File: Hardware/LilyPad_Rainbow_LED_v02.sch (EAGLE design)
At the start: 29 parts

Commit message: Updated Board and Schemtic Files
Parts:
- R1, R2, R3, R4, R5, R6, R7: value 180 -> 150; device SparkFun-Resistors:180OHM1/10W1%(0603) -> SparkFun-Resistors:150OHM-1/10W-1%(0603)
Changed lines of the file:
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@@
 <part name="ST1" library="LilyPad-Wearables" deviceset="SEWTAP" device="6" value="ST +"/>
 <part name="ST" library="LilyPad-Wearables" deviceset="SEWTAP" device="6" value="ST -"/>
-<part name="R1" library="SparkFun-Resistors" deviceset="180OHM1/10W1%(0603)" device="" value="180"/>
+<part name="R1" library="SparkFun-Resistors" deviceset="150OHM-1/10W-1%(0603)" device="" value="150"/>
 <part name="D1" library="SparkFun-LED" deviceset="LED-WHITE" device="1206" value="WHITE"/>
 <part name="ST2" library="LilyPad-Wearables" deviceset="SEWTAP" device="6" value="ST +"/>
 <part name="ST3" library="LilyPad-Wearables" deviceset="SEWTAP" device="6" value="ST -"/>
-<part name="R2" library="SparkFun-Resistors" deviceset="180OHM1/10W1%(0603)" device="" value="180"/>
+<part name="R2" library="SparkFun-Resistors" deviceset="150OHM-1/10W-1%(0603)" device="" value="150"/>
 <part name="D2" library="SparkFun-LED" deviceset="LED-PINK" device="1206" value="PINK"/>
 <part name="ST4" library="LilyPad-Wearables" deviceset="SEWTAP" device="6" value="ST +"/>
 <part name="ST5" library="LilyPad-Wearables" deviceset="SEWTAP" device="6" value="ST -"/>
-<part name="R3" library="SparkFun-Resistors" deviceset="180OHM1/10W1%(0603)" device="" value="180"/>
+<part name="R3" library="SparkFun-Resistors" deviceset="150OHM-1/10W-1%(0603)" device="" value="150"/>
 <part name="D3" library="SparkFun-LED" deviceset="LED-RED" device="LILYPAD" value="RED"/>
 <part name="ST6" library="LilyPad-Wearables" deviceset="SEWTAP" device="6" value="ST +"/>
 <part name="ST7" library="LilyPad-Wearables" deviceset="SEWTAP" device="6" value="ST -"/>
-<part name="R4" library="SparkFun-Resistors" deviceset="180OHM1/10W1%(0603)" device="" value="180"/>
+<part name="R4" library="SparkFun-Resistors" deviceset="150OHM-1/10W-1%(0603)" device="" value="150"/>
 <part name="D4" library="SparkFun-LED" deviceset="LED-YELLOW" device="LILYPAD" value="Yellow"/>
 <part name="ST8" library="LilyPad-Wearables" deviceset="SEWTAP" device="6" value="ST +"/>
 <part name="ST9" library="LilyPad-Wearables" deviceset="SEWTAP" device="6" value="ST -"/>
-<part name="R5" library="SparkFun-Resistors" deviceset="180OHM1/10W1%(0603)" device="" value="180"/>
+<part name="R5" library="SparkFun-Resistors" deviceset="150OHM-1/10W-1%(0603)" device="" value="150"/>
 <part name="D5" library="SparkFun-LED" deviceset="LED-GREEN" device="LILYPAD" value="GREEN"/>
 <part name="ST10" library="LilyPad-Wearables" deviceset="SEWTAP" device="6" value="ST +"/>
 <part name="ST11" library="LilyPad-Wearables" deviceset="SEWTAP" device="6" value="ST -"/>
-<part name="R6" library="SparkFun-Resistors" deviceset="180OHM1/10W1%(0603)" device="" value="180"/>
+<part name="R6" library="SparkFun-Resistors" deviceset="150OHM-1/10W-1%(0603)" device="" value="150"/>
 <part name="D6" library="SparkFun-LED" deviceset="LED-BLUE" device="1206" value="BLUE"/>
 <part name="ST12" library="LilyPad-Wearables" deviceset="SEWTAP" device="6" value="ST +"/>
 <part name="ST13" library="LilyPad-Wearables" deviceset="SEWTAP" device="6" value="ST -"/>
-<part name="R7" library="SparkFun-Resistors" deviceset="180OHM1/10W1%(0603)" device="" value="180"/>
+<part name="R7" library="SparkFun-Resistors" deviceset="150OHM-1/10W-1%(0603)" device="" value="150"/>
 <part name="D7" library="SparkFun-LED" deviceset="LED-WHITE" device="1206" value="WHITE"/>
 <part name="FRAME1" library="SparkFun-Aesthetics" deviceset="FRAME-LETTER" device=""/>

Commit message: updated Board and Schematic files
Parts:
- added U$1: REVISION, SparkFun-Aesthetics:REVISION
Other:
- note added: "Leah Buechley"
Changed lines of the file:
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@@
 <part name="D7" library="SparkFun-LED" deviceset="LED-WHITE" device="1206" value="WHITE"/>
 <part name="FRAME1" library="SparkFun-Aesthetics" deviceset="FRAME-LETTER" device=""/>
+<part name="U$1" library="SparkFun-Aesthetics" deviceset="REVISION" device=""/>
 </parts>
 <sheets>
@@
 <plain>
 <text x="121.92" y="106.68" size="3.81" layer="97" font="vector"></text>
-<text x="167.64" y="10.16" size="2.54" layer="94">Mary West </text>
+<text x="171.45" y="7.62" size="2.54" layer="94">Mary West </text>
 <text x="238.76" y="7.62" size="1.778" layer="94">v02</text>
+<text x="166.37" y="11.43" size="2.54" layer="94">Leah Buechley</text>
 </plain>
 <instances>
@@
 <instance part="FRAME1" gate="G$1" x="0" y="0"/>
 <instance part="FRAME1" gate="V" x="147.32" y="0"/>
+<instance part="U$1" gate="G$1" x="149.86" y="7.62"/>
 </instances>
 <busses>

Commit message: updated fies
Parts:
- added LOGO1: OSHW-LOGOM-COPPER, SparkFun-Aesthetics:OSHW-LOGOM-COPPER
- added LOGO2: SFE_LOGO_NAME_FLAME.1_INCH, SparkFun-Aesthetics:SFE_LOGO_NAME_FLAME.1_INCH
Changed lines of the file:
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@@
 <part name="FRAME1" library="SparkFun-Aesthetics" deviceset="FRAME-LETTER" device=""/>
 <part name="U$1" library="SparkFun-Aesthetics" deviceset="REVISION" device=""/>
+<part name="LOGO2" library="SparkFun-Aesthetics" deviceset="SFE_LOGO_NAME_FLAME" device=".1_INCH"/>
+<part name="LOGO1" library="SparkFun-Aesthetics" deviceset="OSHW-LOGO" device="M-COPPER"/>
 </parts>
 <sheets>
@@
 <instance part="FRAME1" gate="V" x="147.32" y="0"/>
 <instance part="U$1" gate="G$1" x="149.86" y="7.62"/>
+<instance part="LOGO2" gate="G$1" x="165.1" y="35.56"/>
+<instance part="LOGO1" gate="G$1" x="233.68" y="48.26"/>
 </instances>
 <busses>

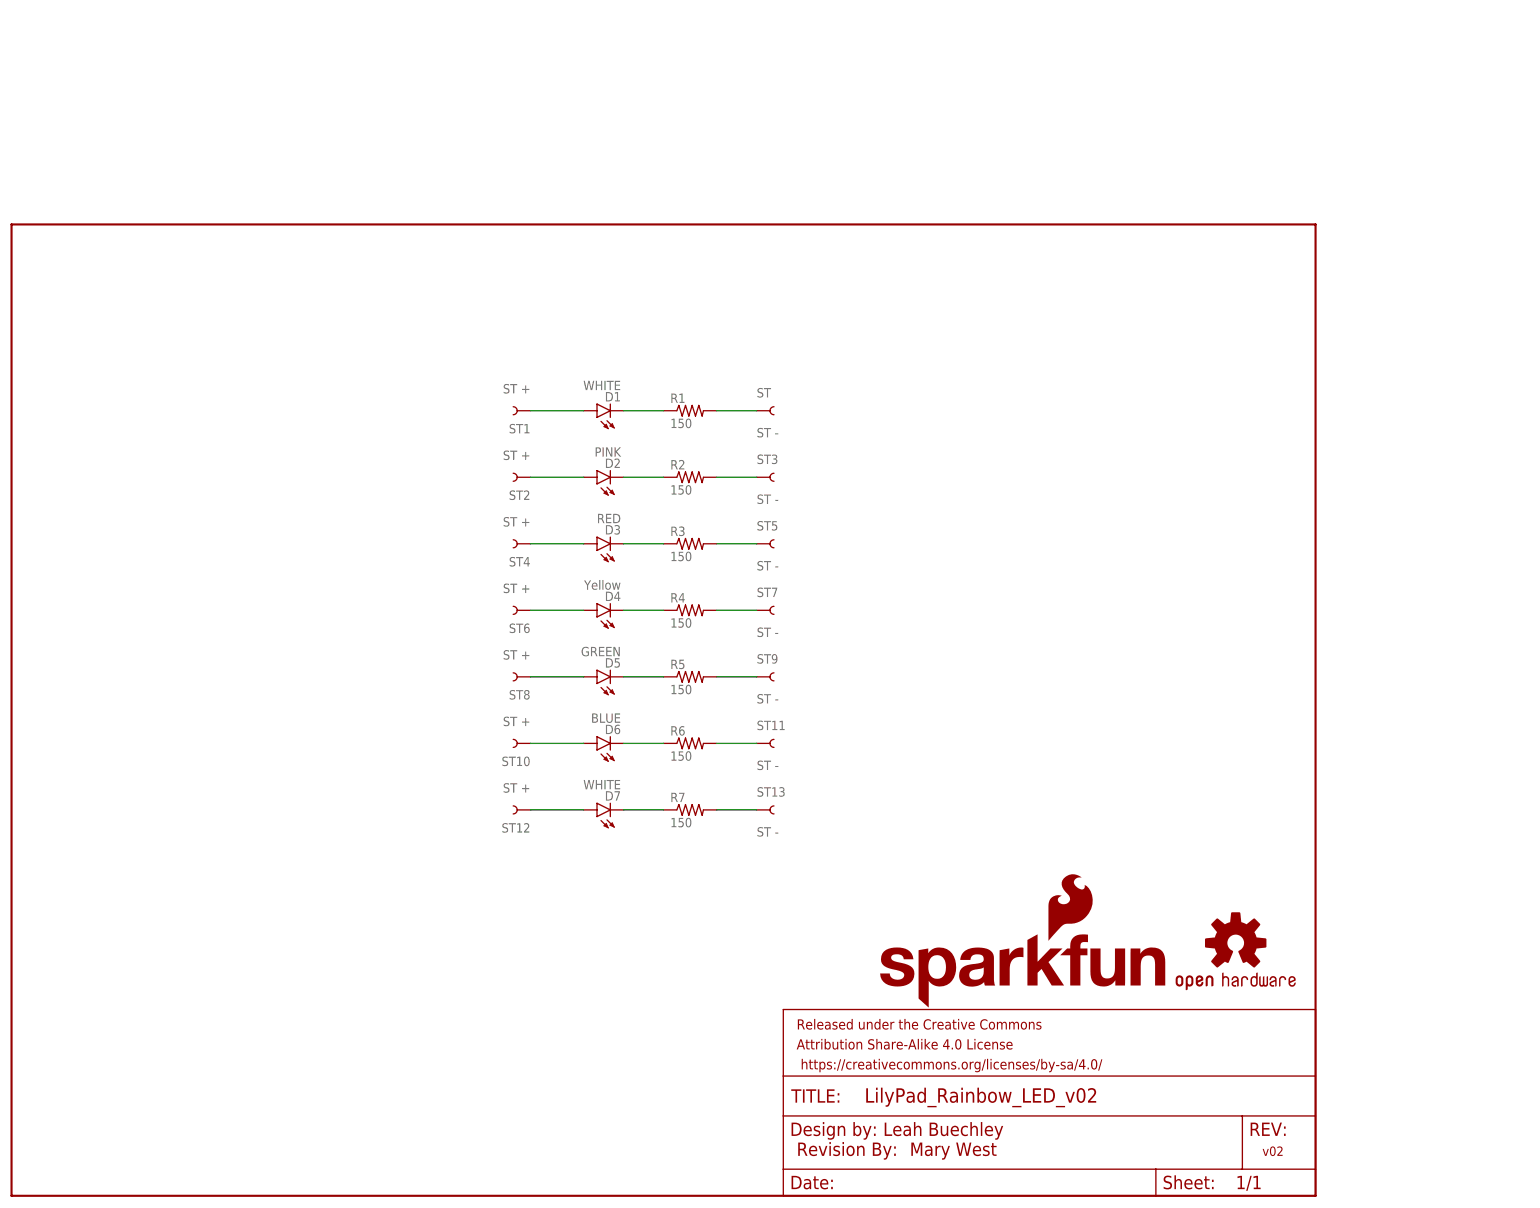
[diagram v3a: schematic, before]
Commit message: Board and Schematic files are Consistent
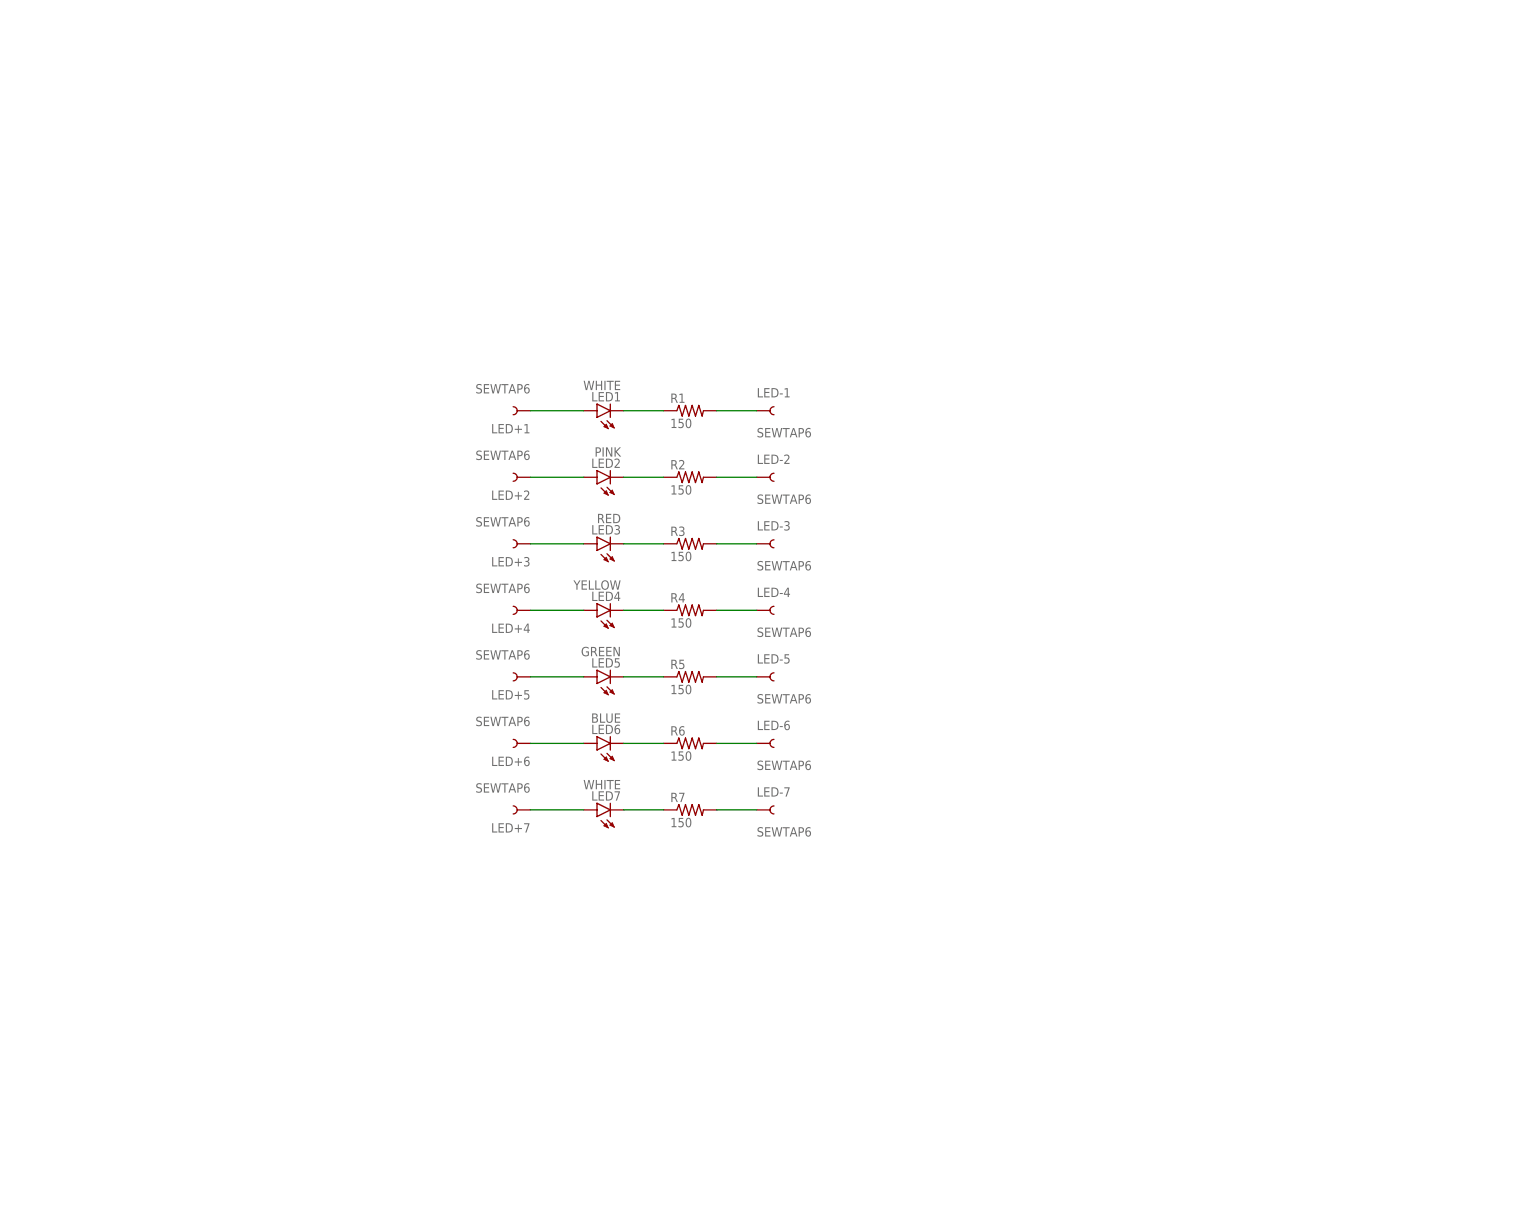
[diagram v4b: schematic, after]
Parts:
- removed FRAME1: FRAME-LETTER, SparkFun-Aesthetics:FRAME-LETTER
- removed LOGO1: OSHW-LOGOM-COPPER, SparkFun-Aesthetics:OSHW-LOGOM-COPPER
- removed LOGO2: SFE_LOGO_NAME_FLAME.1_INCH, SparkFun-Aesthetics:SFE_LOGO_NAME_FLAME.1_INCH
- removed U$1: REVISION, SparkFun-Aesthetics:REVISION
- LED+1, LED+2, LED+3, LED+4, LED+5, LED+6, LED+7: value ST + -> SEWTAP6
- LED-1, LED-2, LED-3, LED-4, LED-5, LED-6, LED-7: value ST - -> SEWTAP6
- LED4: value Yellow -> YELLOW
- renumbered D1 to LED1, D2 to LED2, D3 to LED3, D4 to LED4, D5 to LED5, D6 to LED6, D7 to LED7, ST to LED-1, ST1 to LED+1, ST10 to LED+6, ST11 to LED-6, ST12 to LED+7, ST13 to LED-7, ST2 to LED+2, ST3 to LED-2, ST4 to LED+3, ST5 to LED-3, ST6 to LED+4, ST7 to LED-4, ST8 to LED+5, ST9 to LED-5
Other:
- note removed: "Leah Buechley"
- note removed: "Mary West"
- note removed: "v02"

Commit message: updated Brd and Sch files (in Sync)
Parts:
- added FRAME1: FRAME-LETTER, SparkFun-Aesthetics:FRAME-LETTER
- added U$1: REVISION, SparkFun-Aesthetics:REVISION
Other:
- note added: "L. Buechley"
- note added: "M. West"
- note added: "v02"
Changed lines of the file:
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@@
 <part name="R7" library="SparkFun-Resistors" deviceset="150OHM-1/10W-1%(0603)" device="" value="150"/>
 <part name="LED7" library="SparkFun-LED" deviceset="LED-WHITE" device="1206" value="WHITE"/>
+<part name="FRAME1" library="SparkFun-Aesthetics" deviceset="FRAME-LETTER" device=""/>
+<part name="U$1" library="SparkFun-Aesthetics" deviceset="REVISION" device=""/>
 </parts>
 <sheets>
@@
 <plain>
 <text x="121.92" y="106.68" size="3.81" layer="97" font="vector"></text>
+<text x="207.264" y="52.578" size="2.54" layer="94" font="vector">L. Buechley </text>
+<text x="210.82" y="48.26" size="2.54" layer="94" font="vector">M. West</text>
+<text x="279.4" y="48.26" size="1.778" layer="94">v02</text>
 </plain>
 <instances>
@@
 <instance part="R7" gate="G$1" x="129.54" y="73.66"/>
 <instance part="LED7" gate="G$1" x="111.76" y="73.66" rot="R90"/>
+<instance part="FRAME1" gate="G$1" x="40.64" y="40.64"/>
+<instance part="FRAME1" gate="V" x="187.96" y="40.64"/>
+<instance part="U$1" gate="G$1" x="189.23" y="47.244"/>
 </instances>
 <busses>

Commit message: updated version number and approved DRC errors
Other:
- note added: "v11"
- note removed: "v02"
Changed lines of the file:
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@@
 <text x="207.264" y="52.578" size="2.54" layer="94" font="vector">L. Buechley </text>
 <text x="210.82" y="48.26" size="2.54" layer="94" font="vector">M. West</text>
-<text x="279.4" y="48.26" size="1.778" layer="94">v02</text>
+<text x="279.4" y="48.26" size="1.778" layer="94">v11</text>
 </plain>
 <instances>

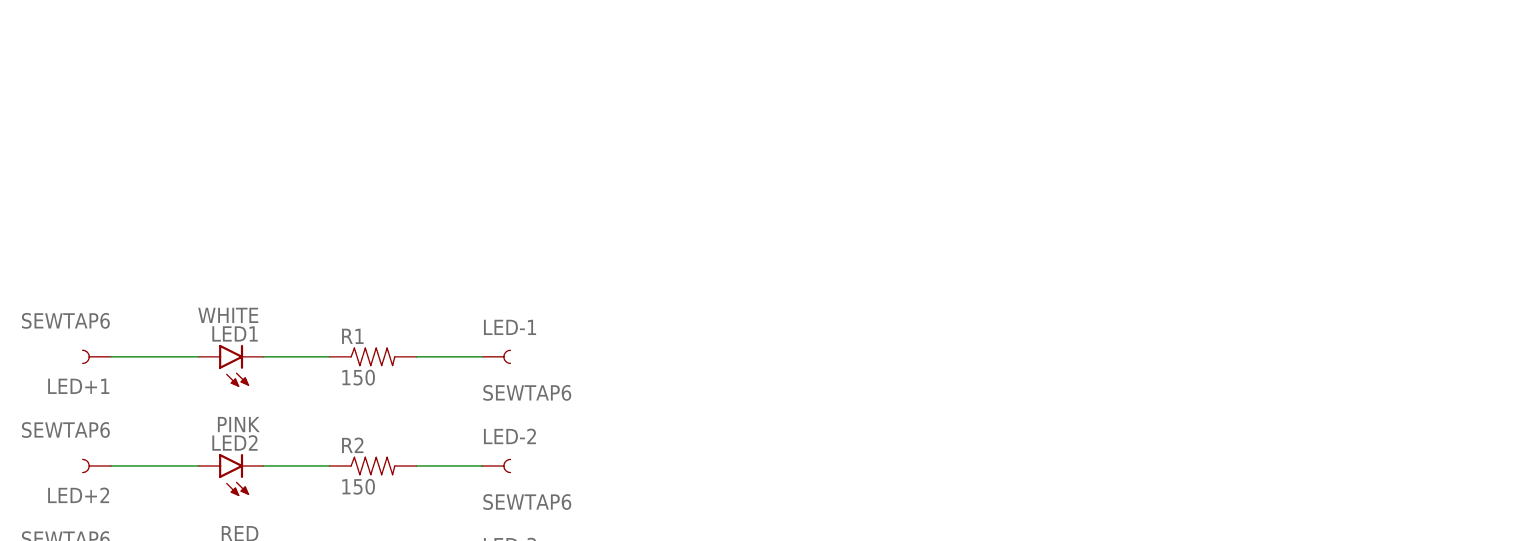
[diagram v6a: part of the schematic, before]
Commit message: Updated Board File and Sch File per Eng. Design Review
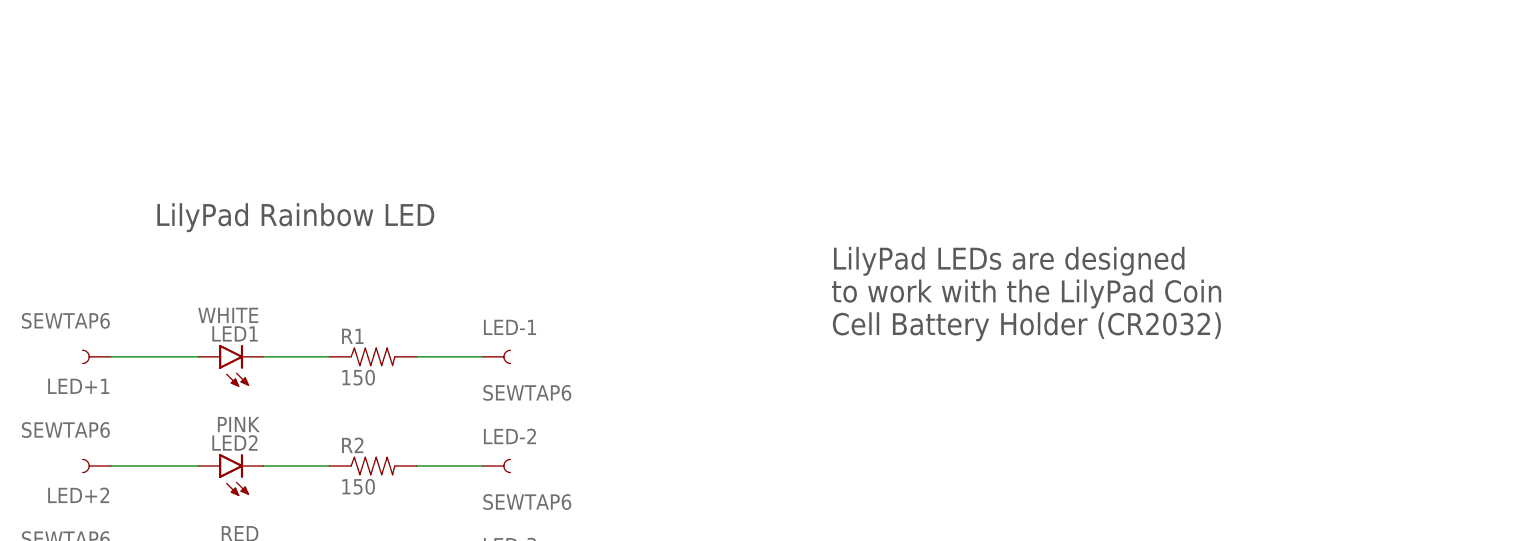
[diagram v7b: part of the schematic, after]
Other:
- note added: "LilyPad LEDs are designed to work with the LilyPad Coin Cell Battery Holder (CR2032)"
- note added: "LilyPad Rainbow LED"
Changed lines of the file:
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@@
 <text x="210.82" y="48.26" size="2.54" layer="94" font="vector">M. West</text>
 <text x="279.4" y="48.26" size="1.778" layer="94">v11</text>
+<text x="104.14" y="165.1" size="2.54" layer="97" font="vector">LilyPad Rainbow LED</text>
+<text x="182.88" y="152.4" size="2.54" layer="97" font="vector">LilyPad LEDs are designed
+to work with the LilyPad Coin
+Cell Battery Holder (CR2032)</text>
 </plain>
 <instances>
@@
 </schematic>
 </drawing>
+<compatibility>
+<note version="6.3" minversion="6.2.2" severity="warning">
+Since Version 6.2.2 text objects can contain more than one line,
+which will not be processed correctly with this version.
+</note>
+</compatibility>
 </eagle>
